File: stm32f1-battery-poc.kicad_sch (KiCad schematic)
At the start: 133 parts, among them J1 Conn_01x02, J10 Conn_02x02_Odd_Even, J11 Conn_02x02_Odd_Even, J2 Conn_02x07_Odd_Even, J3 Conn_01x02, J7 Conn_02x02_Odd_Even, J8 Conn_02x03_Odd_Even, J9 Conn_02x03_Odd_Even, M1 Motor_3_Phases, M2 Stepper_Motor_bipolar, Q1 Q_NMOS, Q2 Q_NMOS, SW1 SW_Push, SW2 SW_Push, SW3 SW_SPST, SW4 SW_Push, U1 LM78M05, U10 DRV8424RGER, U2 HT753-1, U3 SN65HVD230, U4 DRV8311H, U5 STM32F103C8Tx, U6 QRE1113GR, U7 QRE1113GR, U8 QRE1113GR, U9 BQ77905, Y1 8M

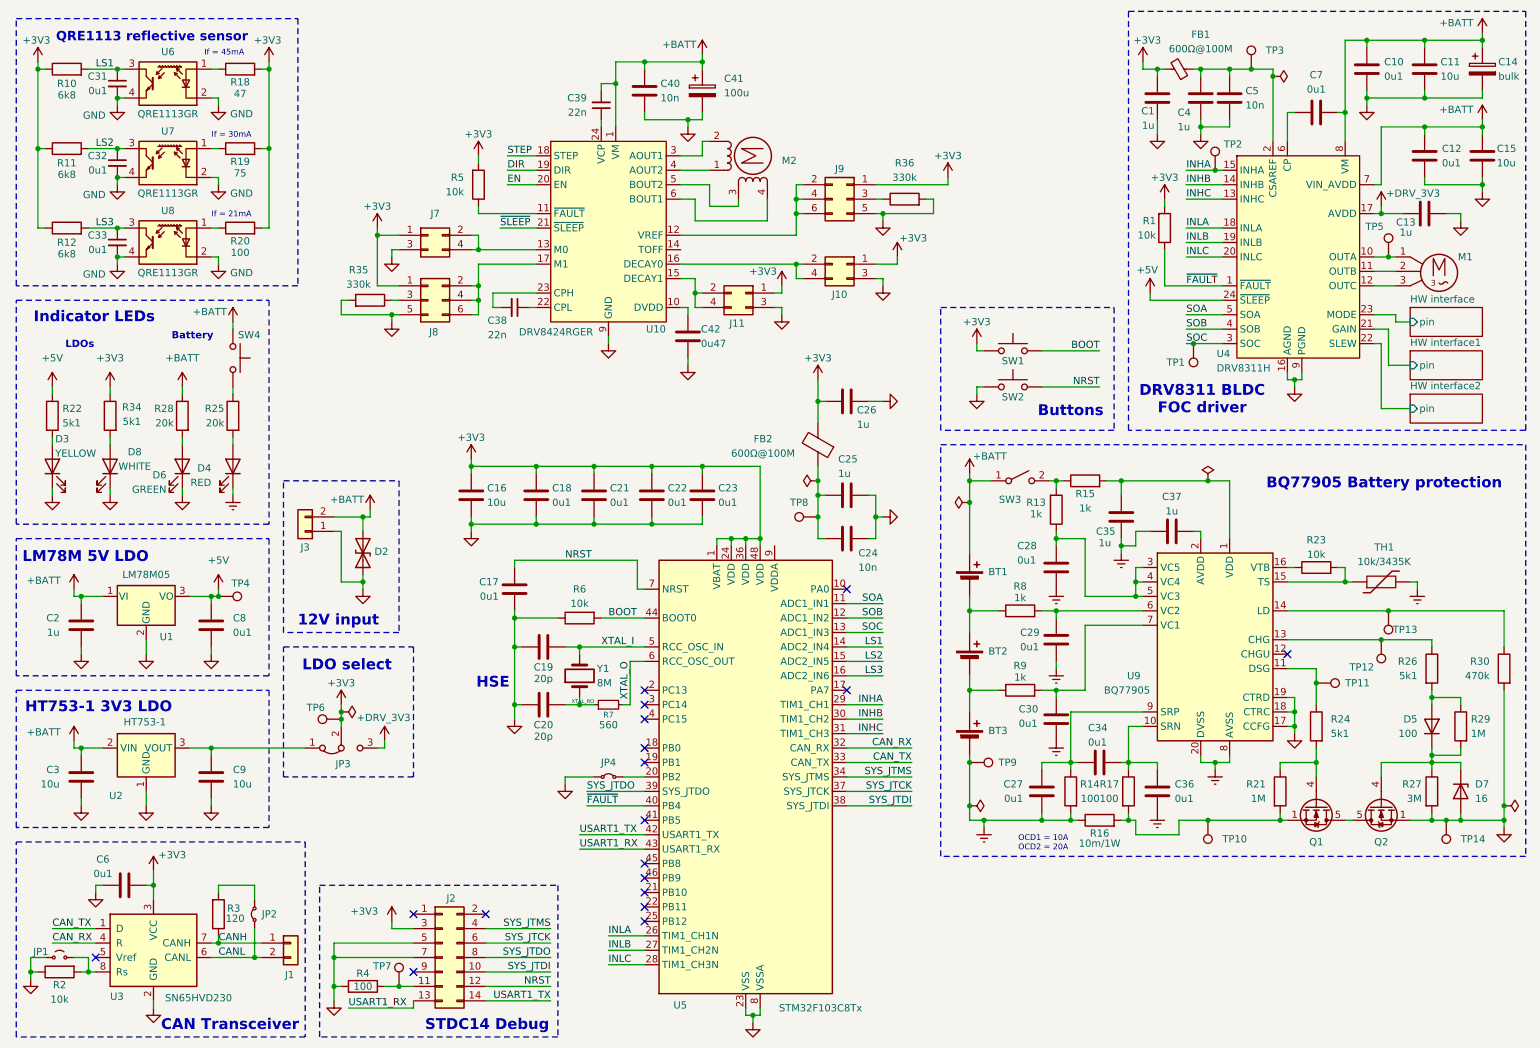
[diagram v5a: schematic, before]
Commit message: schem: add I2C connector
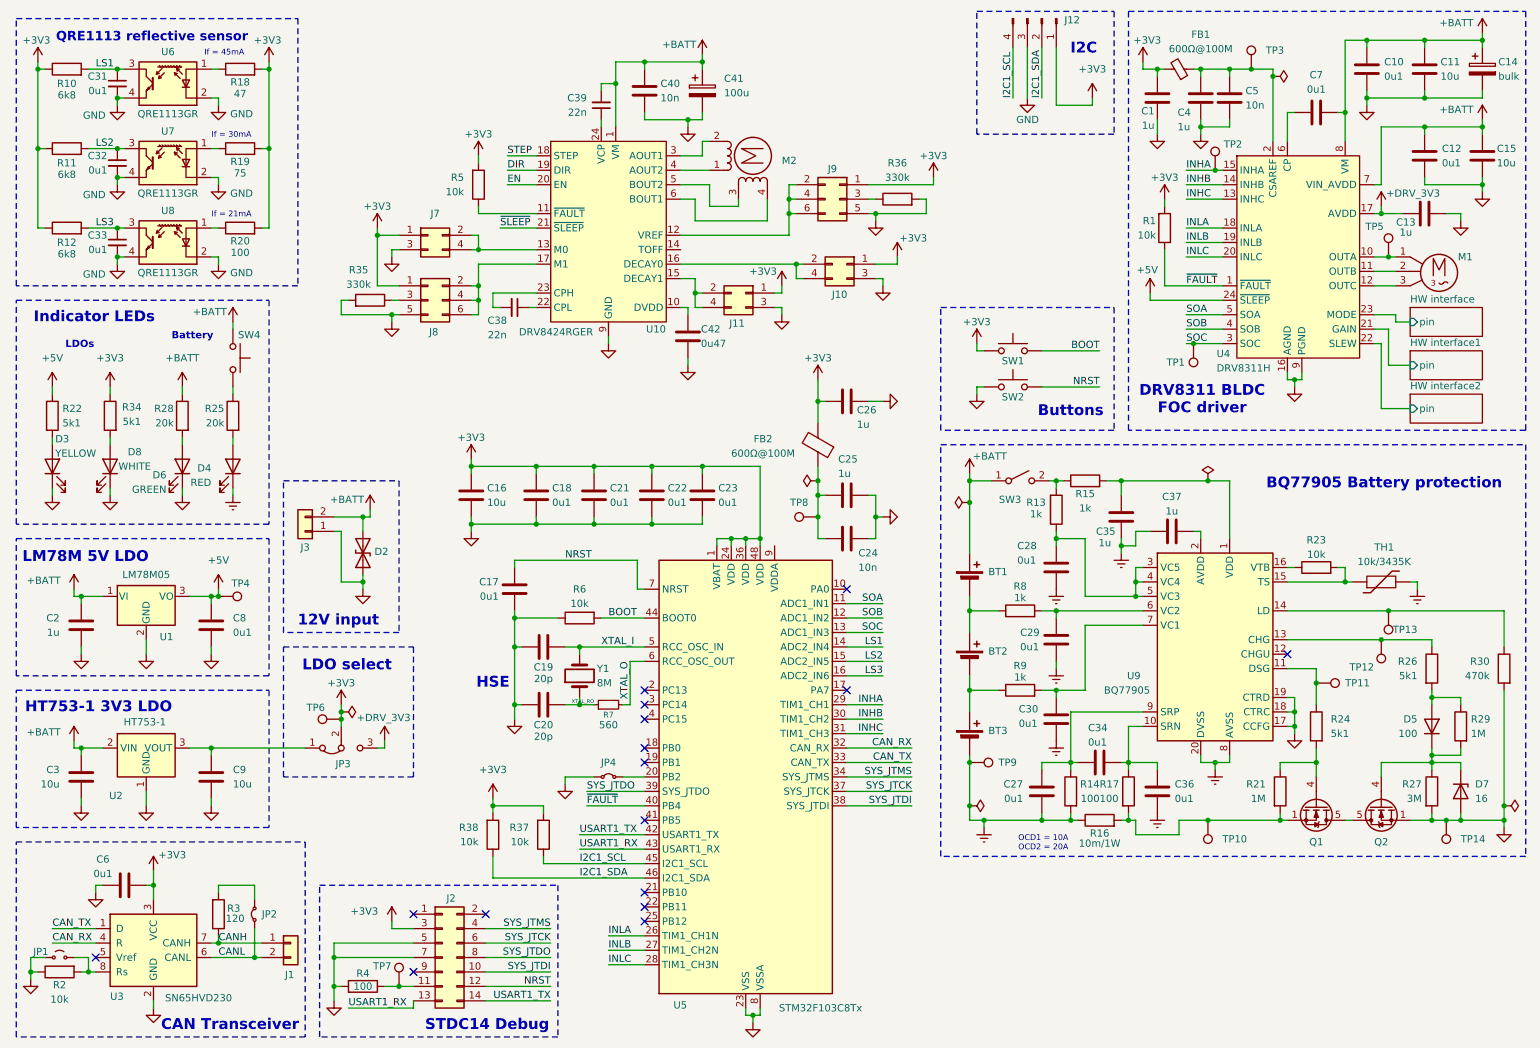
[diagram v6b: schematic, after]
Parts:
- added J12: Conn_01x04_Pin, Connector_PinHeader_2.54mm:PinHeader_1x04_P2.54mm_Vertical, symbol Connector:Conn_01x04_Pin
- added R37, R38: 10k, symbol Device:R
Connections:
- net +3V3: now also J12.1 (Pin_1), R37.2, R38.2
- net EPAD: now also J12.3 (Pin_3)
- net I2C1_SCL: now reaches U5.45 (PB8)
- net I2C1_SCL: now also J12.4 (Pin_4), R37.1
- net I2C1_SDA: now reaches U5.46 (PB9)
- net I2C1_SDA: now also J12.2 (Pin_2), R38.1
- no-connect marks 18 -> 16
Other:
- note added: "I2C"
- moved on the sheet: J9, R36

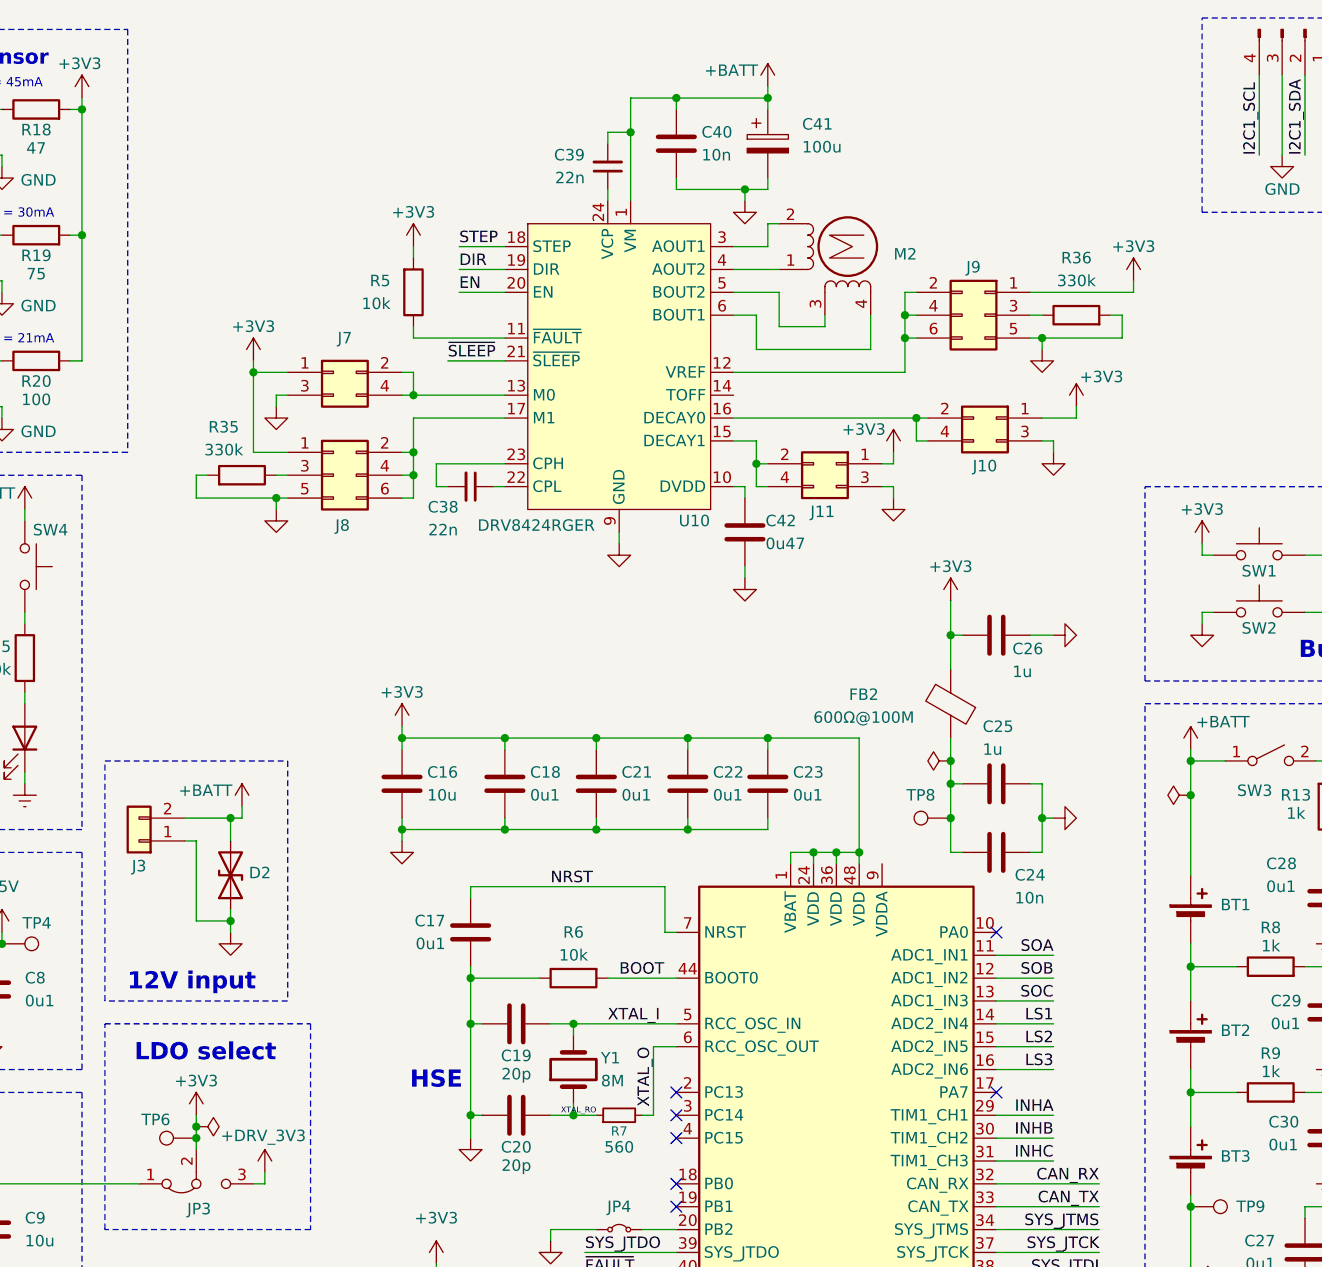
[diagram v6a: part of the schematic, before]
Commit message: schema: connect DRV8424 vref pin
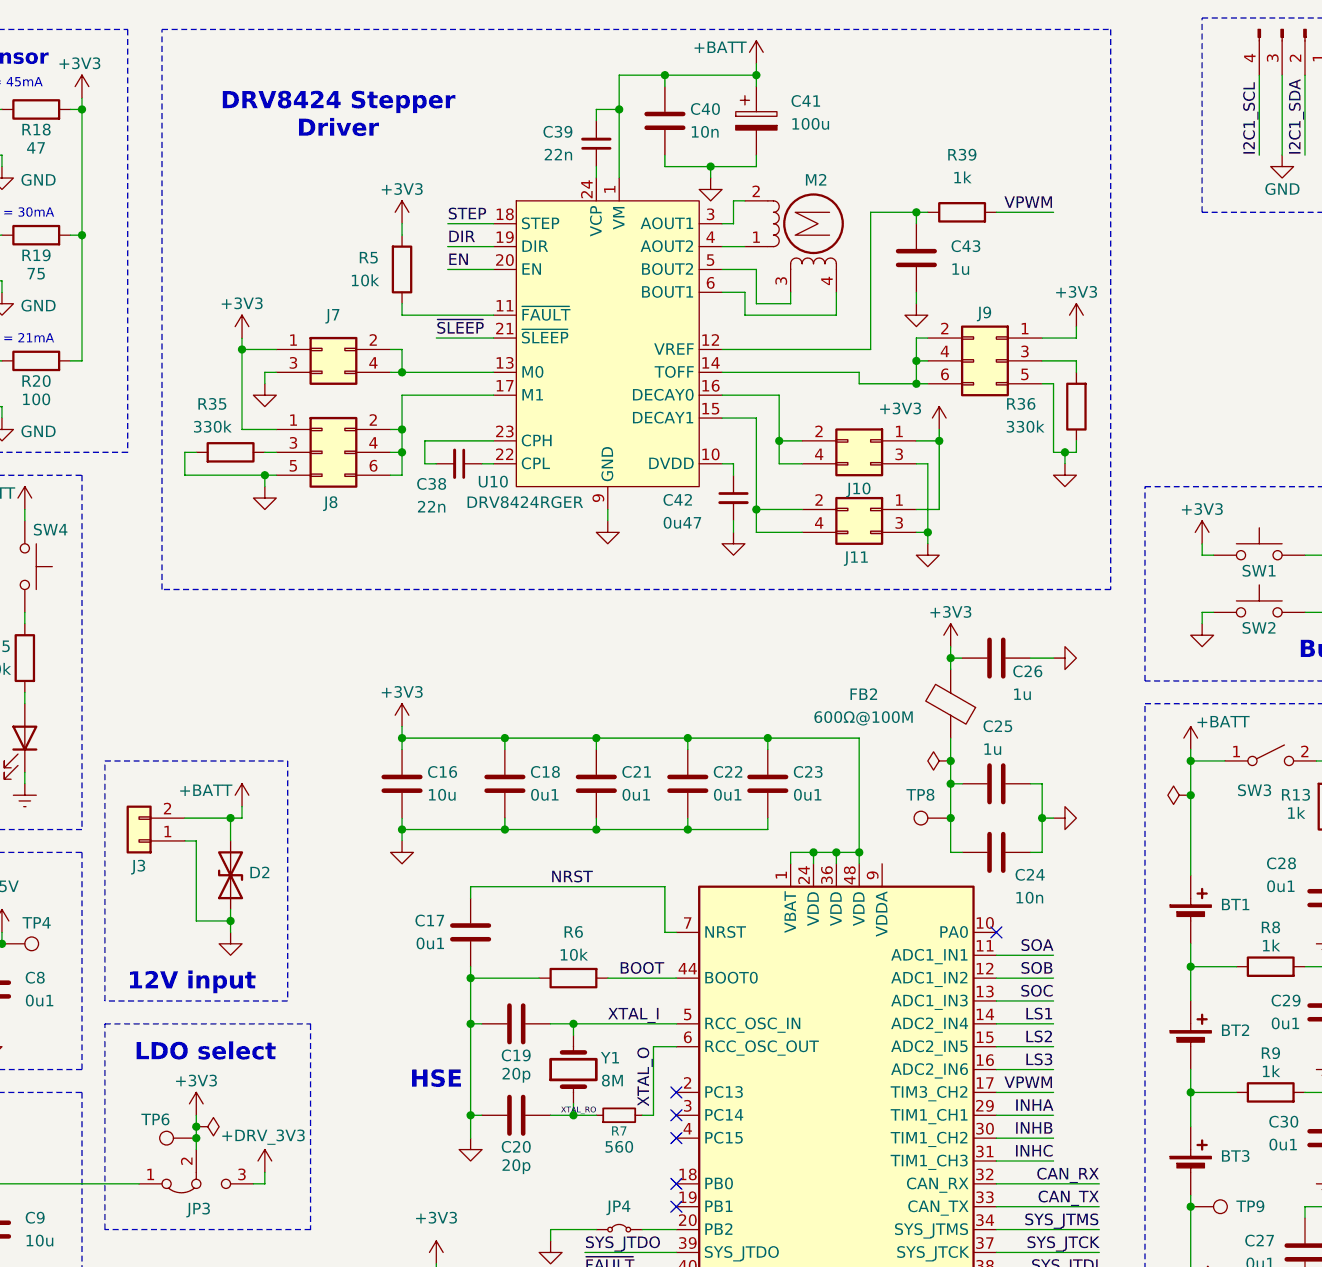
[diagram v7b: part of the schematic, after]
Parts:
- added C43: 1u, symbol Device:C
- added R39: 1k, symbol Device:R
- C42: symbol Device:C -> Device:C_Small
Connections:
- net EPAD: now also R36.1, C43.2; no longer R36.2
- net VPWM: now reaches U5.17 (PA7)
- net VPWM: now also R39.2
- net at J9.3 (Pin_3): now also R36.2; no longer R36.1
- net at J9.2 (Pin_2), J9.4 (Pin_4), J9.6 (Pin_6): now also U10.14 (TOFF); no longer U10.12 (VREF)
- new net: C43.1, R39.1, U10.12 (VREF)
- no-connect marks 16 -> 15
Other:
- note added: "DRV8424 Stepper Driver"
- moved on the sheet: C26, C38, C39, C40, C41, C42, J10, J11, J7, J8, J9, M2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
